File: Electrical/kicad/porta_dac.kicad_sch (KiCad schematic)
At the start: 1 part, among them IC1 ESP32-S3

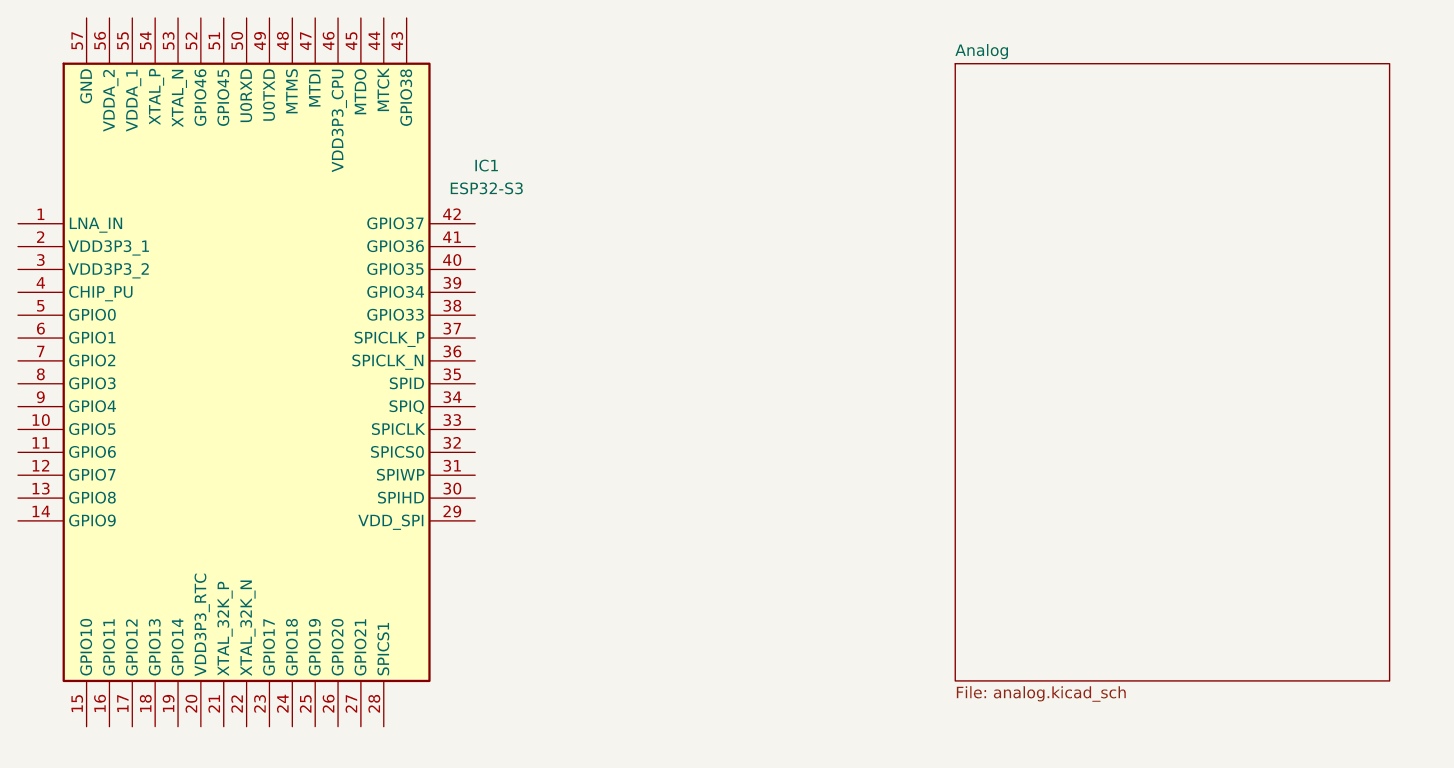
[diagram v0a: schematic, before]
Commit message: Updated PCM1795 schematic sheet
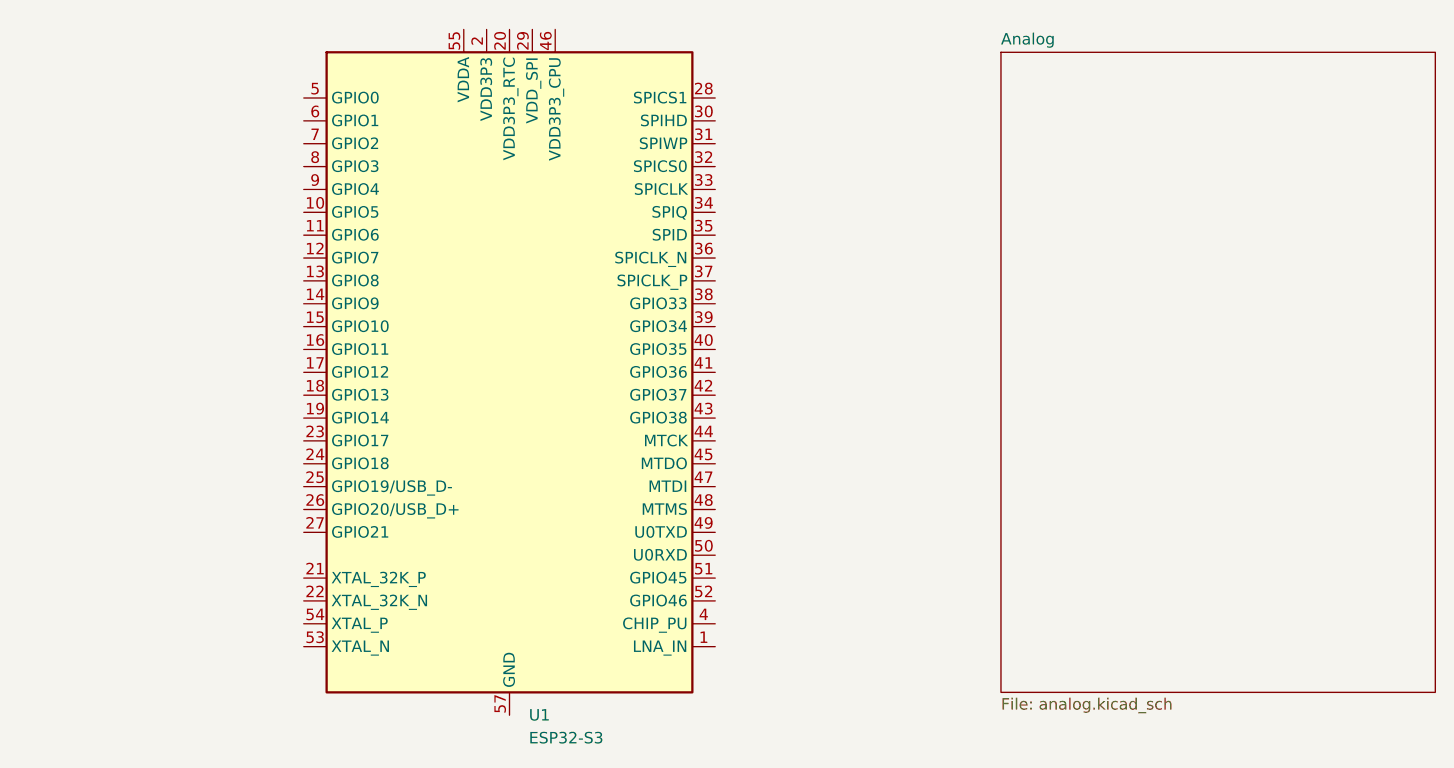
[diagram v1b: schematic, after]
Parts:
- removed IC1: ESP32-S3, QFN40P700X700X90-57N-D, symbol Project_Library:ESP32-S3
- added U1: ESP32-S3, Package_DFN_QFN:QFN-56-1EP_7x7mm_P0.4mm_EP4x4mm, symbol MCU_Espressif:ESP32-S3
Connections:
- new net: U1.2 (VDD3P3), U1.3 (VDD3P3)
- new net: U1.55 (VDDA), U1.56 (VDDA)
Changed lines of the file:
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@@
 	(paper "A4")
 	(symbol
-		(lib_id "Project_Library:ESP32-S3")
-		(at 111.76 83.82 0)
+		(lib_id "MCU_Espressif:ESP32-S3")
+		(at 166.37 100.33 0)
 		(unit 1)
 		(exclude_from_sim no)
@@
 		(dnp no)
 		(fields_autoplaced yes)
-		(property "Reference" "IC1"
-			(at 163.83 77.3998 0)
-			(effects
-				(font
-					(size 1.27 1.27)
-				)
+		(property "Reference" "U1"
+			(at 168.5133 138.43 0)
+			(effects
+				(font
+					(size 1.27 1.27)
+				)
+				(justify left)
 			)
 		)
 		(property "Value" "ESP32-S3"
-			(at 163.83 79.9398 0)
-			(effects
-				(font
-					(size 1.27 1.27)
-				)
-			)
-		)
-		(property "Footprint" "QFN40P700X700X90-57N-D"
-			(at 158.75 163.5 0)
-			(effects
-				(font
-					(size 1.27 1.27)
-				)
-				(justify left top)
+			(at 168.5133 140.97 0)
+			(effects
+				(font
+					(size 1.27 1.27)
+				)
+				(justify left)
+			)
+		)
+		(property "Footprint" "Package_DFN_QFN:QFN-56-1EP_7x7mm_P0.4mm_EP4x4mm"
+			(at 166.37 148.59 0)
+			(effects
+				(font
+					(size 1.27 1.27)
+				)
 				(hide yes)
 			)
 		)
-		(property "Datasheet" ""
-			(at 158.75 263.5 0)
-			(effects
-				(font
-					(size 1.27 1.27)
-				)
-				(justify left top)
+		(property "Datasheet" "https://www.espressif.com/sites/default/files/documentation/esp32-s3_datasheet_en.pdf"
+			(at 166.37 100.33 0)
+			(effects
+				(font
+					(size 1.27 1.27)
+				)
 				(hide yes)
 			)
 		)
-		(property "Description" "WiFi Modules - 802.11 [ENGINEERING SAMPLES]SMD IC, Dual-Core MCU, Wi-Fi 2.4G & BLE 5.0 Combo"
-			(at 111.76 83.82 0)
+		(property "Description" "Microcontroller, Wi-Fi 802.11b/g/n, Bluetooth, 32bit"
+			(at 166.37 100.33 0)
 			(effects
 				(font
@@
 			)
 		)
-		(property "Height" "0.9"
-			(at 158.75 463.5 0)
-			(effects
-				(font
-					(size 1.27 1.27)
-				)
-				(justify left top)
-				(hide yes)
-			)
-		)
-		(property "Mouser Part Number" "356-ESP32-S3"
-			(at 158.75 563.5 0)
-			(effects
-				(font
-					(size 1.27 1.27)
-				)
-				(justify left top)
-				(hide yes)
-			)
-		)
-		(property "Mouser Price/Stock" "https://www.mouser.co.uk/ProductDetail/Espressif-Systems/ESP32-S3?qs=Rp5uXu7WBW%2FNWuUy%252BBihNw%3D%3D"
-			(at 158.75 663.5 0)
-			(effects
-				(font
-					(size 1.27 1.27)
-				)
-				(justify left top)
-				(hide yes)
-			)
-		)
-		(property "Manufacturer_Name" "Espressif Systems"
-			(at 158.75 763.5 0)
-			(effects
-				(font
-					(size 1.27 1.27)
-				)
-				(justify left top)
-				(hide yes)
-			)
-		)
-		(property "Manufacturer_Part_Number" "ESP32-S3"
-			(at 158.75 863.5 0)
-			(effects
-				(font
-					(size 1.27 1.27)
-				)
-				(justify left top)
-				(hide yes)
-			)
+		(pin "56"
+		)
+		(pin "55"
+		)
+		(pin "11"
+		)
+		(pin "20"
+		)
+		(pin "54"
+		)
+		(pin "9"
+		)
+		(pin "46"
+		)
+		(pin "13"
+		)
+		(pin "36"
+		)
+		(pin "22"
+		)
+		(pin "51"
+		)
+		(pin "8"
+		)
+		(pin "6"
+		)
+		(pin "10"
+		)
+		(pin "12"
+		)
+		(pin "17"
+		)
+		(pin "24"
 		)
 		(pin "7"
 		)
+		(pin "14"
+		)
+		(pin "19"
+		)
+		(pin "15"
+		)
+		(pin "25"
+		)
+		(pin "26"
+		)
+		(pin "27"
+		)
+		(pin "45"
+		)
+		(pin "16"
+		)
+		(pin "21"
+		)
+		(pin "23"
+		)
+		(pin "53"
+		)
 		(pin "18"
 		)
-		(pin "51"
+		(pin "5"
+		)
+		(pin "2"
+		)
+		(pin "3"
+		)
+		(pin "57"
+		)
+		(pin "29"
+		)
+		(pin "28"
+		)
+		(pin "34"
+		)
+		(pin "40"
+		)
+		(pin "38"
+		)
+		(pin "47"
+		)
+		(pin "52"
+		)
+		(pin "32"
+		)
+		(pin "31"
+		)
+		(pin "48"
+		)
+		(pin "35"
+		)
+		(pin "30"
+		)
+		(pin "1"
+		)
+		(pin "42"
+		)
+		(pin "41"
+		)
+		(pin "39"
+		)
+		(pin "4"
+		)
+		(pin "44"
+		)
+		(pin "33"
+		)
+		(pin "43"
+		)
+		(pin "37"
 		)
 		(pin "50"
 		)
 		(pin "49"
-		)
-		(pin "6"
-		)
-		(pin "9"
-		)
-		(pin "57"
-		)
-		(pin "8"
-		)
-		(pin "10"
-		)
-		(pin "15"
-		)
-		(pin "56"
-		)
-		(pin "53"
-		)
-		(pin "19"
-		)
-		(pin "1"
-		)
-		(pin "2"
-		)
-		(pin "3"
-		)
-		(pin "4"
-		)
-		(pin "5"
-		)
-		(pin "11"
-		)
-		(pin "12"
-		)
-		(pin "13"
-		)
-		(pin "14"
-		)
-		(pin "55"
-		)
-		(pin "17"
-		)
-		(pin "16"
-		)
-		(pin "54"
-		)
-		(pin "52"
-		)
-		(pin "20"
-		)
-		(pin "21"
-		)
-		(pin "22"
-		)
-		(pin "23"
-		)
-		(pin "48"
-		)
-		(pin "24"
-		)
-		(pin "47"
-		)
-		(pin "25"
-		)
-		(pin "39"
-		)
-		(pin "37"
-		)
-		(pin "26"
-		)
-		(pin "44"
-		)
-		(pin "30"
-		)
-		(pin "29"
-		)
-		(pin "36"
-		)
-		(pin "46"
-		)
-		(pin "33"
-		)
-		(pin "40"
-		)
-		(pin "35"
-		)
-		(pin "41"
-		)
-		(pin "42"
-		)
-		(pin "27"
-		)
-		(pin "38"
-		)
-		(pin "32"
-		)
-		(pin "43"
-		)
-		(pin "28"
-		)
-		(pin "45"
-		)
-		(pin "34"
-		)
-		(pin "31"
 		)
 		(instances
 			(project ""
 				(path "/87976a50-04ff-4f5b-8f98-ac64b0c9e23b"
-					(reference "IC1")
+					(reference "U1")
 					(unit 1)
 				)
@@
 	)
 	(sheet
-		(at 215.9 66.04)
-		(size 48.26 68.58)
+		(at 220.98 64.77)
+		(size 48.26 71.12)
 		(exclude_from_sim no)
 		(in_bom yes)
@@
 		)
 		(property "Sheetname" "Analog"
-			(at 215.9 65.3284 0)
+			(at 220.98 64.0584 0)
 			(effects
 				(font
@@
 		)
 		(property "Sheetfile" "analog.kicad_sch"
-			(at 215.9 135.2046 0)
-			(effects
-				(font
+			(at 220.98 136.4746 0)
+			(effects
+				(font

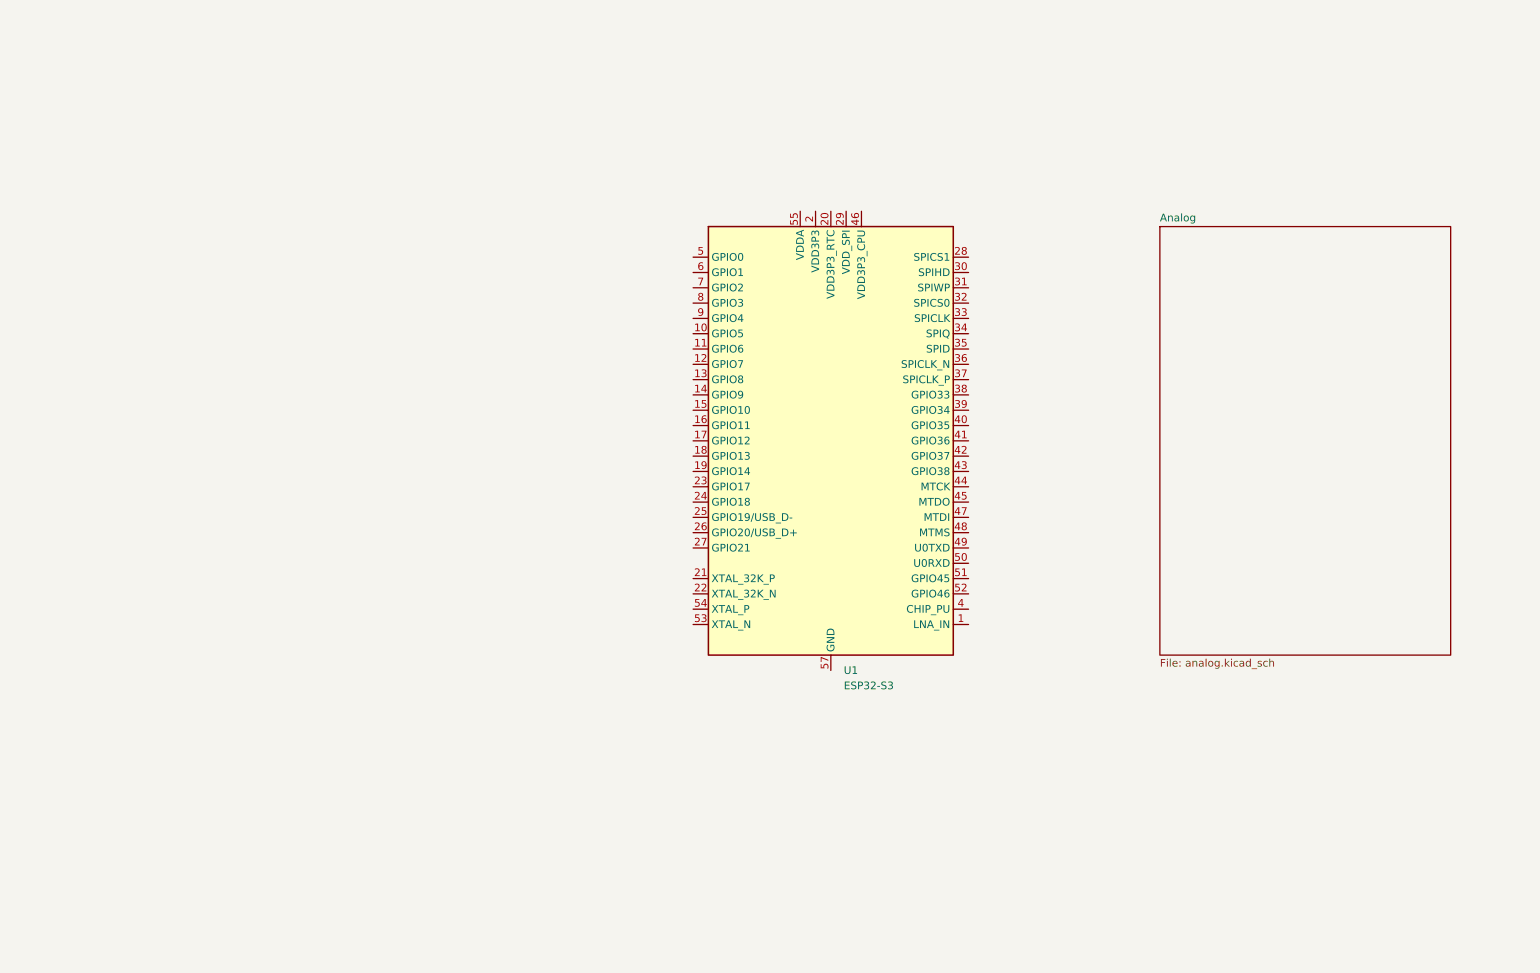
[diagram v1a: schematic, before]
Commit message: Added oscillator and crystal to schematic. Also did some refining of how things were laid out
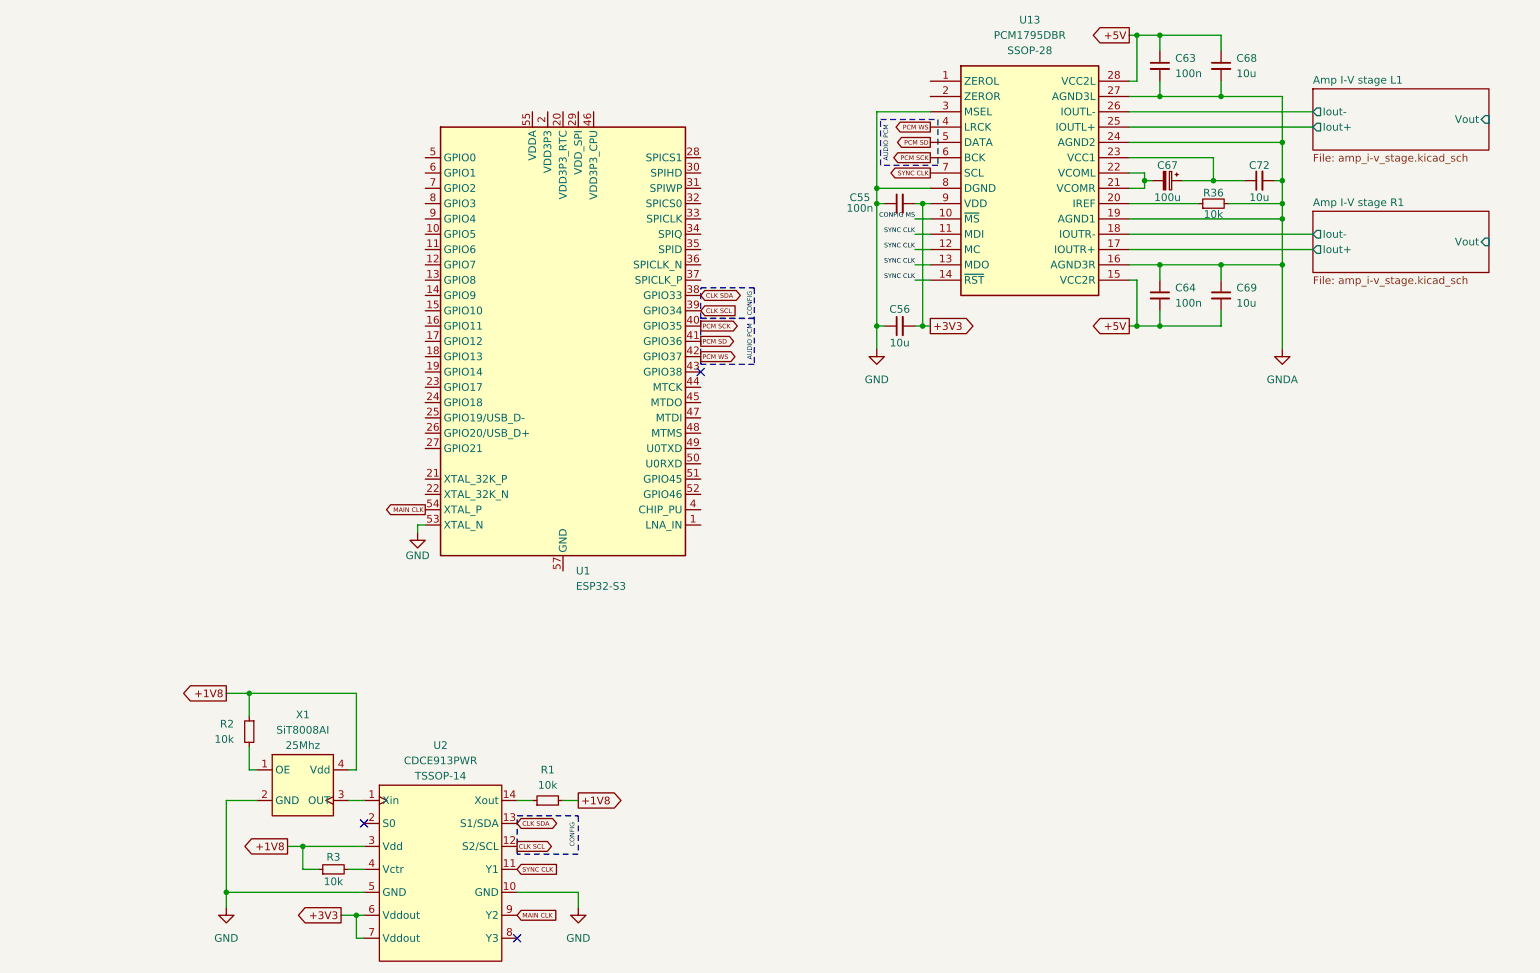
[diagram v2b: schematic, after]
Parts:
- added C55, C63, C64: 100n, Project_Library:PHE426HJ6100JR05, symbol Project_Library:C_100n
- added C56, C68, C69, C72: 10u, Project_Library:CAPC3225X270N, symbol Project_Library:C_10u
- added C67: 100u, Project_Library:CAPPRD350W60D825H1300, symbol Project_Library:C_100u
- added R1, R2, R3, R36: 10k, Project_Library:ERA6AEB101V, symbol Project_Library:R_10k
- added U13: PCM1795DBR, Project_Library:SOP65P780X200-28N, symbol Project_Library:U_PCM1795DBR
- added U2: CDCE913PWR, Project_Library:SOP65P640X120-14N, symbol Project_Library:U_CDCE913PWR
- added X1: SiT8008AI, Project_Library:4L PQFN, symbol Project_Library:X_SiT8008AI-11-18E-25
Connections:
- net CLK SDA: now reaches U1.38 (GPIO33)
- net CLK SDA: now also U2.13 (S1/SDA)
- net CLK SCL: now reaches U1.39 (GPIO34)
- net CLK SCL: now also U2.12 (S2/SCL)
- net PCM SCK: now reaches U1.40 (GPIO35)
- net PCM SCK: now also U13.6 (BCK)
- net PCM SD: now reaches U1.41 (GPIO36)
- net PCM SD: now also U13.5 (DATA)
- net PCM WS: now reaches U1.42 (GPIO37)
- net PCM WS: now also U13.4 (LRCK)
- net GND: now reaches U1.53 (XTAL_N)
- net GND: now also C55.1, C56.1, U13.3 (MSEL), U13.8 (DGND), U2.10 (GND), U2.5 (GND), X1.2 (GND)
- net MAIN CLK: now reaches U1.54 (XTAL_P)
- net MAIN CLK: now also U2.9 (Y2)
- new net: R1.1, U2.14 (Xout)
- new net: R36.1, U13.20 (IREF)
- new net: C67.1, C72.1, U13.23 (VCC1)
- new net: R3.2, U2.4 (Vctr)
- new net: C67.2, U13.21 (VCOMR), U13.22 (VCOML)
- new net: U2.1 (Xin), X1.3 (OUT)
- new net: R2.2, X1.1 (OE)
- new net +1V8: R1.2, R2.1, R3.1, U2.3 (Vdd), X1.4 (Vdd)
- new net +3V3: C55.2, C56.2, U13.9 (VDD), U2.6 (Vddout), U2.7 (Vddout)
- new net +5V: C63.1, C64.2, C68.1, C69.2, U13.15 (VCC2R), U13.28 (VCC2L)
- new net Amp I-V stage L1/Iout+: U13.25 (IOUTL+)
- new net Amp I-V stage L1/Iout-: U13.26 (IOUTL-)
- new net Amp I-V stage R1/Iout+: U13.17 (IOUTR+)
- new net Amp I-V stage R1/Iout-: U13.18 (IOUTR-)
- new net CONFIG MS: U13.10 (~{MS})
- new net GNDA: C63.2, C64.1, C68.2, C69.1, C72.2, R36.2, U13.16 (AGND3R), U13.19 (AGND1), U13.24 (AGND2), U13.27 (AGND3L)
- new net SYNC CLK: U13.11 (MDI), U13.12 (MC), U13.13 (MDO), U13.14 (~{RST}), U13.7 (SCL), U2.11 (Y1)
- no-connect marks 0 -> 3
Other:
- removed sheet Analog
- added sheet Amp I-V stage L1 (amp_i-v_stage.kicad_sch)
- added sheet Amp I-V stage R1 (amp_i-v_stage.kicad_sch)
- note added: "AUDIO PCM"
- note added: "CONFIG"
- moved on the sheet: U1

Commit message: Minor changes
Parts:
- added U3: LT1317IS8, Package_SO:SOIC-8-N7_3.9x4.9mm_P1.27mm, symbol Project_Library:U_LT1317IS8
- added U4: TLV73318PDBV, Package_TO_SOT_SMD:SOT-23-5, symbol Regulator_Linear:TLV73318PDBV
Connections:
- net SYNC CLK: no longer U13.11 (MDI), U13.12 (MC), U13.13 (MDO), U13.14 (~{RST})
- new net AUDIO RST: U13.14 (~{RST})
- new net CONFIG MC: U13.12 (MC)
- new net CONFIG MDI: U13.11 (MDI)
- new net CONFIG MDO: U13.13 (MDO)
- no-connect marks 3 -> 5
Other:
- note added: "CLOCK CONFIG"
- note removed: "CONFIG"
- moved on the sheet: C55, C56
